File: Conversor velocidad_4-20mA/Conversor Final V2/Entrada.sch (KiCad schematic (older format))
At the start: 19 parts

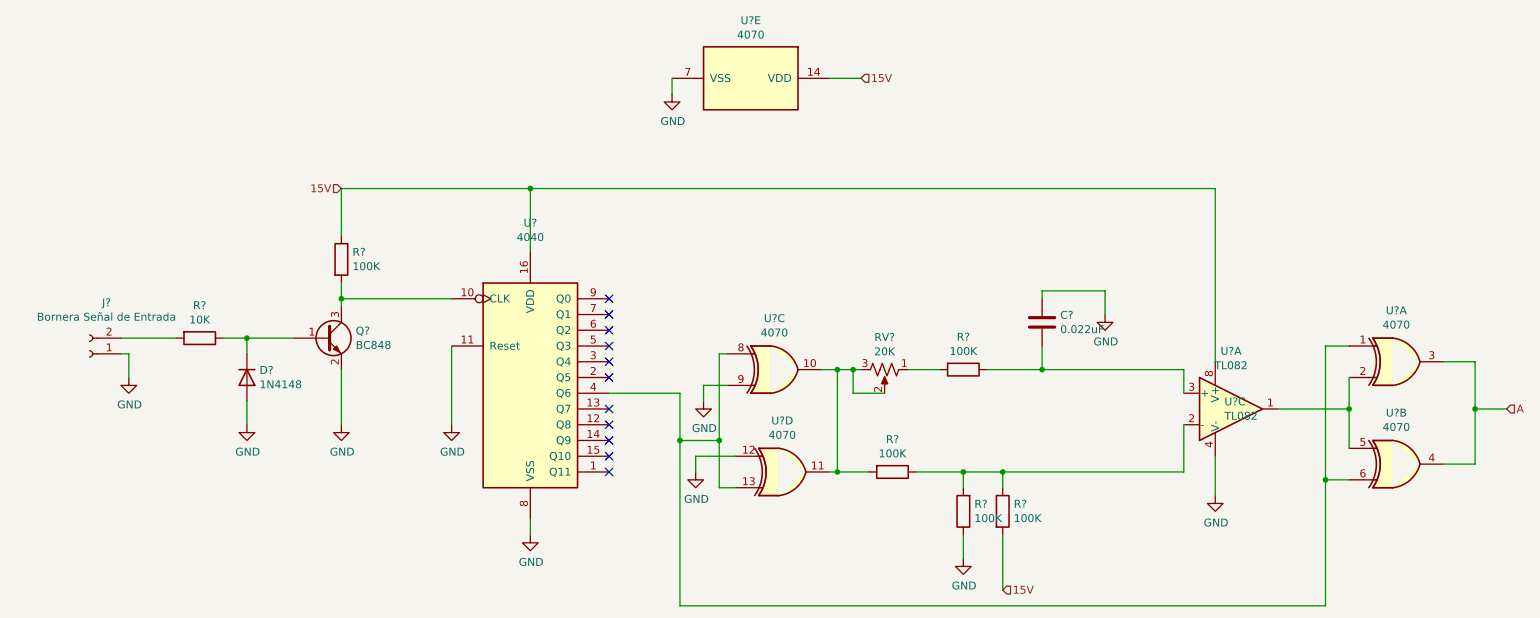
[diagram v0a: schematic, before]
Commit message: Modificacion
Modifique los esquematicos para que no de tanto error. Igualmente da error de puenteo de salidas entre las compuertas "OR" y 2 errores mas en el regulador
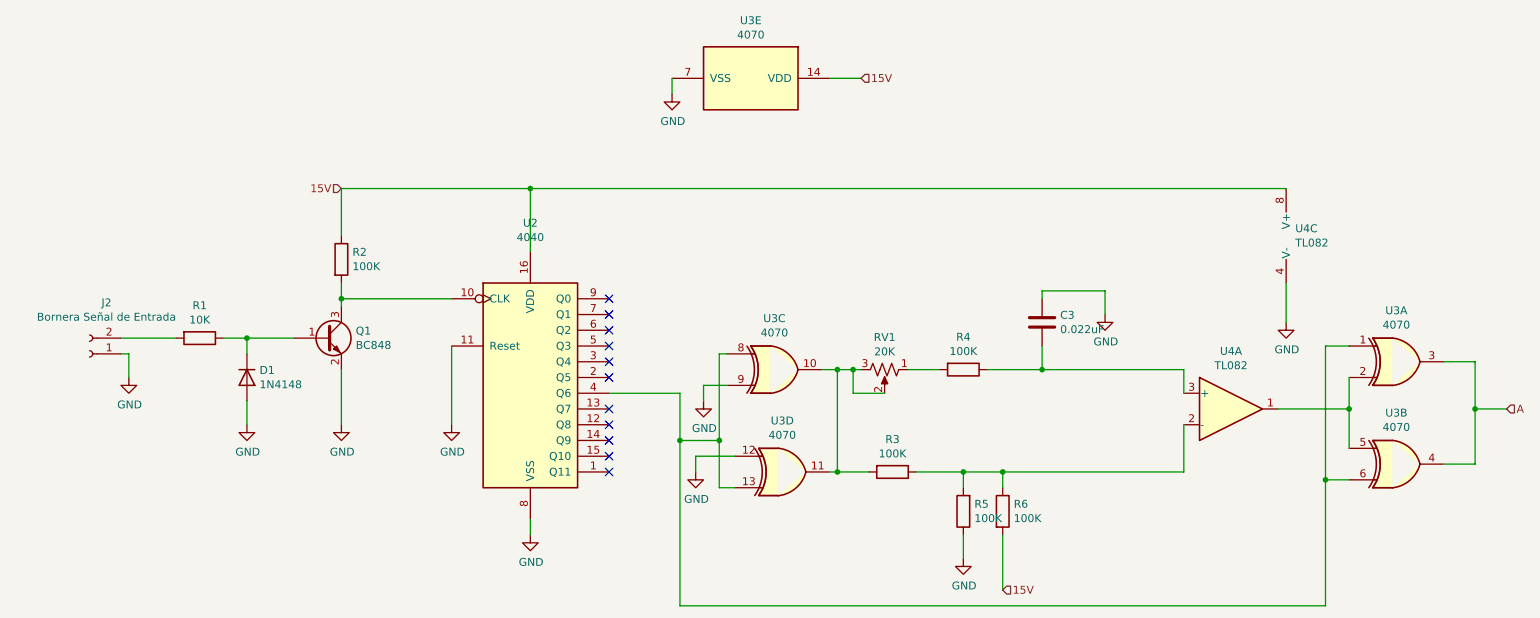
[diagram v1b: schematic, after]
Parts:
- gave numbers to parts that had none: 14
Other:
- moved on the sheet: U4C

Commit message: Agregue footprints
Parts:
- C3: footprint (none) -> Capacitor_SMD:C_0603_1608Metric_Pad1.08x0.95mm_HandSolder
- R1, R2, R3, R4, R5, R6, RV1: footprint (none) -> Resistor_SMD:R_0603_1608Metric_Pad0.98x0.95mm_HandSolder
- U4: footprint (none) -> Package_SO:HSOP-8-1EP_3.9x4.9mm_P1.27mm_EP2.41x3.1mm_ThermalVias
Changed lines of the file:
@@
 F 0 "R2" H 2920 2146 50  0000 L CNN
 F 1 "100K" H 2920 2055 50  0000 L CNN
-F 2 "" V 2780 2100 50  0001 C CNN
+F 2 "Resistor_SMD:R_0603_1608Metric_Pad0.98x0.95mm_HandSolder" V 2780 2100 50  0001 C CNN
 F 3 "~" H 2850 2100 50  0001 C CNN
 	1    2850 2100
@@
 F 0 "R1" V 1743 2600 50  0000 C CNN
 F 1 "10K" V 1834 2600 50  0000 C CNN
-F 2 "" V 1880 2600 50  0001 C CNN
+F 2 "Resistor_SMD:R_0603_1608Metric_Pad0.98x0.95mm_HandSolder" V 1880 2600 50  0001 C CNN
 F 3 "~" H 1950 2600 50  0001 C CNN
 	1    1950 2600
@@
 F 0 "R3" V 6143 3450 50  0000 C CNN
 F 1 "100K" V 6234 3450 50  0000 C CNN
-F 2 "" V 6280 3450 50  0001 C CNN
+F 2 "Resistor_SMD:R_0603_1608Metric_Pad0.98x0.95mm_HandSolder" V 6280 3450 50  0001 C CNN
 F 3 "~" H 6350 3450 50  0001 C CNN
 	1    6350 3450
@@
 F 0 "R5" H 6730 3654 50  0000 R CNN
 F 1 "100K" H 6730 3745 50  0000 R CNN
-F 2 "" V 6730 3700 50  0001 C CNN
+F 2 "Resistor_SMD:R_0603_1608Metric_Pad0.98x0.95mm_HandSolder" V 6730 3700 50  0001 C CNN
 F 3 "~" H 6800 3700 50  0001 C CNN
 	1    6800 3700
@@
 F 0 "R6" H 7120 3746 50  0000 L CNN
 F 1 "100K" H 7120 3655 50  0000 L CNN
-F 2 "" V 6980 3700 50  0001 C CNN
+F 2 "Resistor_SMD:R_0603_1608Metric_Pad0.98x0.95mm_HandSolder" V 6980 3700 50  0001 C CNN
 F 3 "~" H 7050 3700 50  0001 C CNN
 	1    7050 3700
@@
 F 0 "R4" V 6593 2800 50  0000 C CNN
 F 1 "100K" V 6684 2800 50  0000 C CNN
-F 2 "" V 6730 2800 50  0001 C CNN
+F 2 "Resistor_SMD:R_0603_1608Metric_Pad0.98x0.95mm_HandSolder" V 6730 2800 50  0001 C CNN
 F 3 "~" H 6800 2800 50  0001 C CNN
 	1    6800 2800
@@
 F 0 "U4" H 8500 3417 50  0000 C CNN
 F 1 "TL082" H 8500 3326 50  0000 C CNN
-F 2 "" H 8500 3050 50  0001 C CNN
+F 2 "Package_SO:HSOP-8-1EP_3.9x4.9mm_P1.27mm_EP2.41x3.1mm_ThermalVias" H 8500 3050 50  0001 C CNN
 F 3 "http://www.ti.com/lit/ds/symlink/tl081.pdf" H 8500 3050 50  0001 C CNN
 	1    8500 3050
@@
 F 0 "RV1" V 6095 2800 50  0000 C CNN
 F 1 "20K" V 6186 2800 50  0000 C CNN
-F 2 "" H 6300 2800 50  0001 C CNN
+F 2 "Resistor_SMD:R_0603_1608Metric_Pad0.98x0.95mm_HandSolder" H 6300 2800 50  0001 C CNN
 F 3 "~" H 6300 2800 50  0001 C CNN
 	1    6300 2800
@@
 F 0 "C3" H 7415 2546 50  0000 L CNN
 F 1 "0.022uF" H 7415 2455 50  0000 L CNN
-F 2 "" H 7338 2350 50  0001 C CNN
+F 2 "Capacitor_SMD:C_0603_1608Metric_Pad1.08x0.95mm_HandSolder" H 7338 2350 50  0001 C CNN
 F 3 "~" H 7300 2500 50  0001 C CNN
 	1    7300 2500
@@
 F 0 "U4" H 8908 1996 50  0000 L CNN
 F 1 "TL082" H 8908 1905 50  0000 L CNN
-F 2 "" H 8950 1950 50  0001 C CNN
+F 2 "Package_SO:HSOP-8-1EP_3.9x4.9mm_P1.27mm_EP2.41x3.1mm_ThermalVias" H 8950 1950 50  0001 C CNN
 F 3 "http://www.ti.com/lit/ds/symlink/tl081.pdf" H 8950 1950 50  0001 C CNN
 	3    8950 1950

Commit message: Actualizacion Esquematico en bloques
Agregue un par de footprints y acomodé el relé en el bloque correspondiente. Hay que consultar sobre los footprint del 4040 y 4070
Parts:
- RV1: footprint Resistor_SMD:R_0603_1608Metric_Pad0.98x0.95mm_HandSolder -> (none)
- U2: footprint (none) -> Package_SO:SOIC-16_3.9x9.9mm_P1.27mm
- U4: footprint Package_SO:HSOP-8-1EP_3.9x4.9mm_P1.27mm_EP2.41x3.1mm_ThermalVias -> Package_SO:SOIC-8-1EP_3.9x4.9mm_P1.27mm_EP2.29x3mm
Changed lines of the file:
@@
 F 0 "U2" H 4050 3831 50  0000 C CNN
 F 1 "4040" H 4050 3740 50  0000 C CNN
-F 2 "" H 4050 2850 50  0001 C CNN
-F 3 "http://www.intersil.com/content/dam/Intersil/documents/cd40/cd4020bms-24bms-40bms.pdf" H 4050 2850 50  0001 C CNN
+F 2 "Package_SO:SOIC-16_3.9x9.9mm_P1.27mm" H 4050 2850 50  0001 C CNN
+F 3 "https://www.digikey.com/es/products/detail/texas-instruments/CD4040BM/1691010" H 4050 2850 50  0001 C CNN
 	1    4050 2850
 	1    0    0    -1
@@
 F 1 "4070" H 9550 2984 50  0000 C CNN
 F 2 "" H 9550 2750 50  0001 C CNN
-F 3 "http://www.intersil.com/content/dam/Intersil/documents/cd40/cd4070bms-77bms.pdf" H 9550 2750 50  0001 C CNN
+F 3 "https://www.digikey.com/es/products/detail/texas-instruments/CD4070BMT/1691302" H 9550 2750 50  0001 C CNN
 	1    9550 2750
 	1    0    0    -1
@@
 F 1 "4070" H 9550 3634 50  0000 C CNN
 F 2 "" H 9550 3400 50  0001 C CNN
-F 3 "http://www.intersil.com/content/dam/Intersil/documents/cd40/cd4070bms-77bms.pdf" H 9550 3400 50  0001 C CNN
+F 3 "https://www.digikey.com/es/products/detail/texas-instruments/CD4070BMT/1691302" H 9550 3400 50  0001 C CNN
 	2    9550 3400
 	1    0    0    -1
@@
 F 1 "4070" H 5600 3034 50  0000 C CNN
 F 2 "" H 5600 2800 50  0001 C CNN
-F 3 "http://www.intersil.com/content/dam/Intersil/documents/cd40/cd4070bms-77bms.pdf" H 5600 2800 50  0001 C CNN
+F 3 "https://www.digikey.com/es/products/detail/texas-instruments/CD4070BMT/1691302" H 5600 2800 50  0001 C CNN
 	3    5600 2800
 	1    0    0    -1
@@
 F 1 "4070" V 5174 950 50  0000 C CNN
 F 2 "" H 5450 950 50  0001 C CNN
-F 3 "http://www.intersil.com/content/dam/Intersil/documents/cd40/cd4070bms-77bms.pdf" H 5450 950 50  0001 C CNN
+F 3 "https://www.digikey.com/es/products/detail/texas-instruments/CD4070BMT/1691302" H 5450 950 50  0001 C CNN
 	5    5450 950
 	0    1    1    0
@@
 F 0 "U4" H 8500 3417 50  0000 C CNN
 F 1 "TL082" H 8500 3326 50  0000 C CNN
-F 2 "Package_SO:HSOP-8-1EP_3.9x4.9mm_P1.27mm_EP2.41x3.1mm_ThermalVias" H 8500 3050 50  0001 C CNN
+F 2 "Package_SO:SOIC-8-1EP_3.9x4.9mm_P1.27mm_EP2.29x3mm" H 8500 3050 50  0001 C CNN
 F 3 "http://www.ti.com/lit/ds/symlink/tl081.pdf" H 8500 3050 50  0001 C CNN
 	1    8500 3050
@@
 F 0 "RV1" V 6095 2800 50  0000 C CNN
 F 1 "20K" V 6186 2800 50  0000 C CNN
-F 2 "Resistor_SMD:R_0603_1608Metric_Pad0.98x0.95mm_HandSolder" H 6300 2800 50  0001 C CNN
+F 2 "" H 6300 2800 50  0001 C CNN
 F 3 "~" H 6300 2800 50  0001 C CNN
 	1    6300 2800
@@
 F 1 "4070" H 5650 3684 50  0000 C CNN
 F 2 "" H 5650 3450 50  0001 C CNN
-F 3 "http://www.intersil.com/content/dam/Intersil/documents/cd40/cd4070bms-77bms.pdf" H 5650 3450 50  0001 C CNN
+F 3 "https://www.digikey.com/es/products/detail/texas-instruments/CD4070BMT/1691302" H 5650 3450 50  0001 C CNN
 	4    5650 3450
 	1    0    0    -1
@@
 F 0 "U4" H 8908 1996 50  0000 L CNN
 F 1 "TL082" H 8908 1905 50  0000 L CNN
-F 2 "Package_SO:HSOP-8-1EP_3.9x4.9mm_P1.27mm_EP2.41x3.1mm_ThermalVias" H 8950 1950 50  0001 C CNN
+F 2 "Package_SO:SOIC-8-1EP_3.9x4.9mm_P1.27mm_EP2.29x3mm" H 8950 1950 50  0001 C CNN
 F 3 "http://www.ti.com/lit/ds/symlink/tl081.pdf" H 8950 1950 50  0001 C CNN
 	3    8950 1950
